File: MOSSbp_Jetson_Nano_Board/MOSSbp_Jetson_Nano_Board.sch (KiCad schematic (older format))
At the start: 13 parts, among them J1 24V, J2 Jetson_Nano_Dev, U1 LMR14020

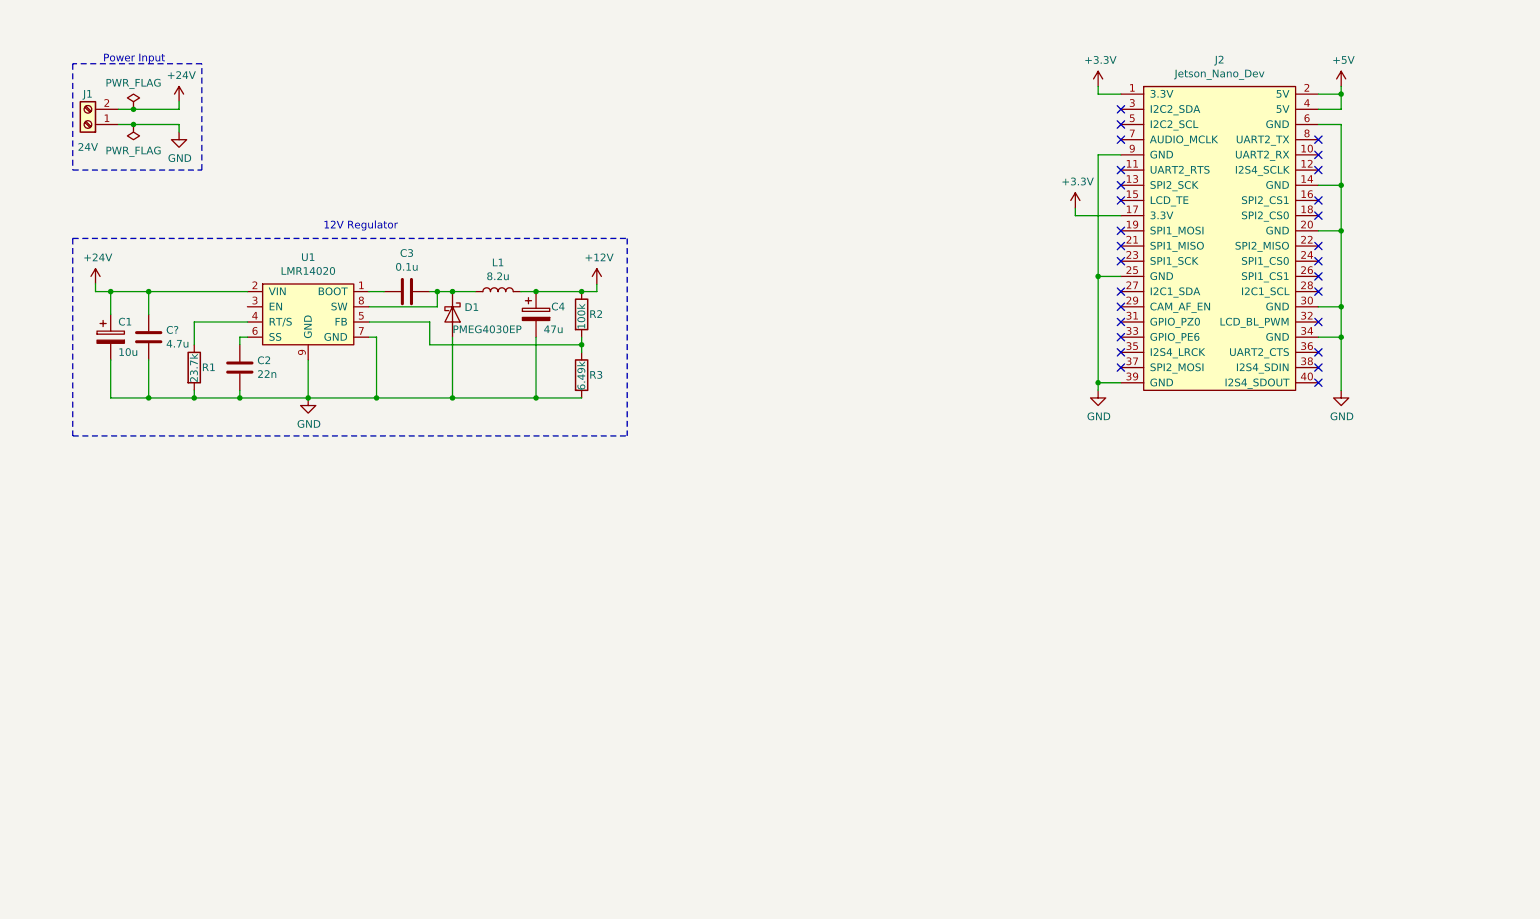
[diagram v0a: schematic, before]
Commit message: Added fans and pump controls
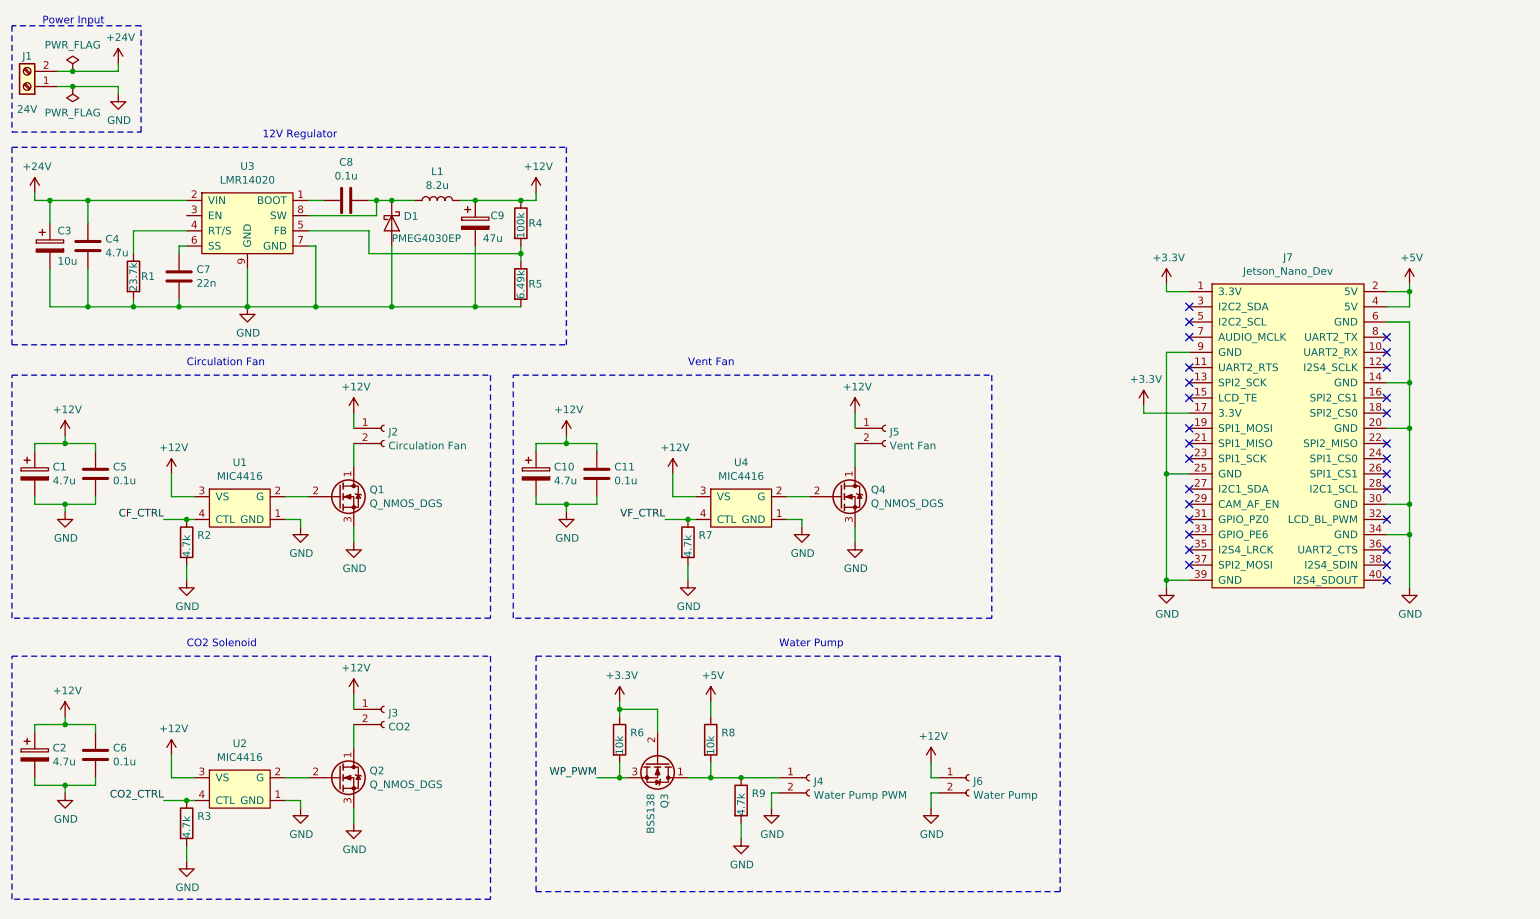
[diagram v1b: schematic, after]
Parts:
- added C1, C10, C2: 4.7u, symbol Device:CP
- added C11, C5, C6: 0.1u, symbol Device:C
- added J2: Circulation Fan, symbol Connector:Conn_01x02_Female
- added J3: CO2, symbol Connector:Conn_01x02_Female
- added J4: Water Pump PWM, symbol Connector:Conn_01x02_Female
- added J5: Vent Fan, symbol Connector:Conn_01x02_Female
- added J6: Water Pump, symbol Connector:Conn_01x02_Female
- added Q1, Q2, Q4: Q_NMOS_DGS, symbol Device:Q_NMOS_DGS
- added Q3: BSS138, symbol Device:Q_NMOS_DGS
- added R2, R3, R7, R9: 4.7k, symbol Device:R
- added R6, R8: 10k, symbol Device:R
- added U1, U2, U4: MIC4416, Package_TO_SOT_SMD:SOT-143, symbol rg_symbols:MIC4416
- gave numbers to parts that had none: 1
- renumbered C1 to C3, C2 to C7, C3 to C8, C4 to C9, J2 to J7, R2 to R4, R3 to R5, U1 to U3
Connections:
- net +12V: now also C1.1, C10.1, C11.1, C2.1, C5.1, C6.1, J2.1 (Pin_1), J3.1 (Pin_1), J5.1 (Pin_1), J6.1 (Pin_1), U1.3 (VS), U2.3 (VS), U4.3 (VS)
- net +3V3: now also Q3.2 (G), R6.1
- net +5V: now also R8.1
- net GND: now also C1.2, C10.2, C11.2, C2.2, C5.2, C6.2, J4.2 (Pin_2), J6.2 (Pin_2), Q1.3 (S), Q2.3 (S), Q4.3 (S), R2.2, R3.2, R7.2, R9.2, U1.1 (GND), U2.1 (GND), U4.1 (GND)
- new net: J2.2 (Pin_2), Q1.1 (D)
- new net: Q1.2 (G), U1.2 (G)
- new net: J5.2 (Pin_2), Q4.1 (D)
- new net: Q4.2 (G), U4.2 (G)
- new net: J3.2 (Pin_2), Q2.1 (D)
- new net: Q2.2 (G), U2.2 (G)
- new net: J4.1 (Pin_1), Q3.1 (D), R8.2, R9.1
- new net CF_CTRL: R2.1, U1.4 (CTL)
- new net CO2_CTRL: R3.1, U2.4 (CTL)
- new net VF_CTRL: R7.1, U4.4 (CTL)
- new net WP_PWM: Q3.3 (S), R6.2
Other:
- note added: "CO2 Solenoid"
- note added: "Circulation Fan"
- note added: "Vent Fan"
- note added: "Water Pump"
- moved on the sheet: C3, C4, C7, C8, C9, D1, J1, J7, L1, R1, R4, R5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

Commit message: Added 5V regulator and control pins
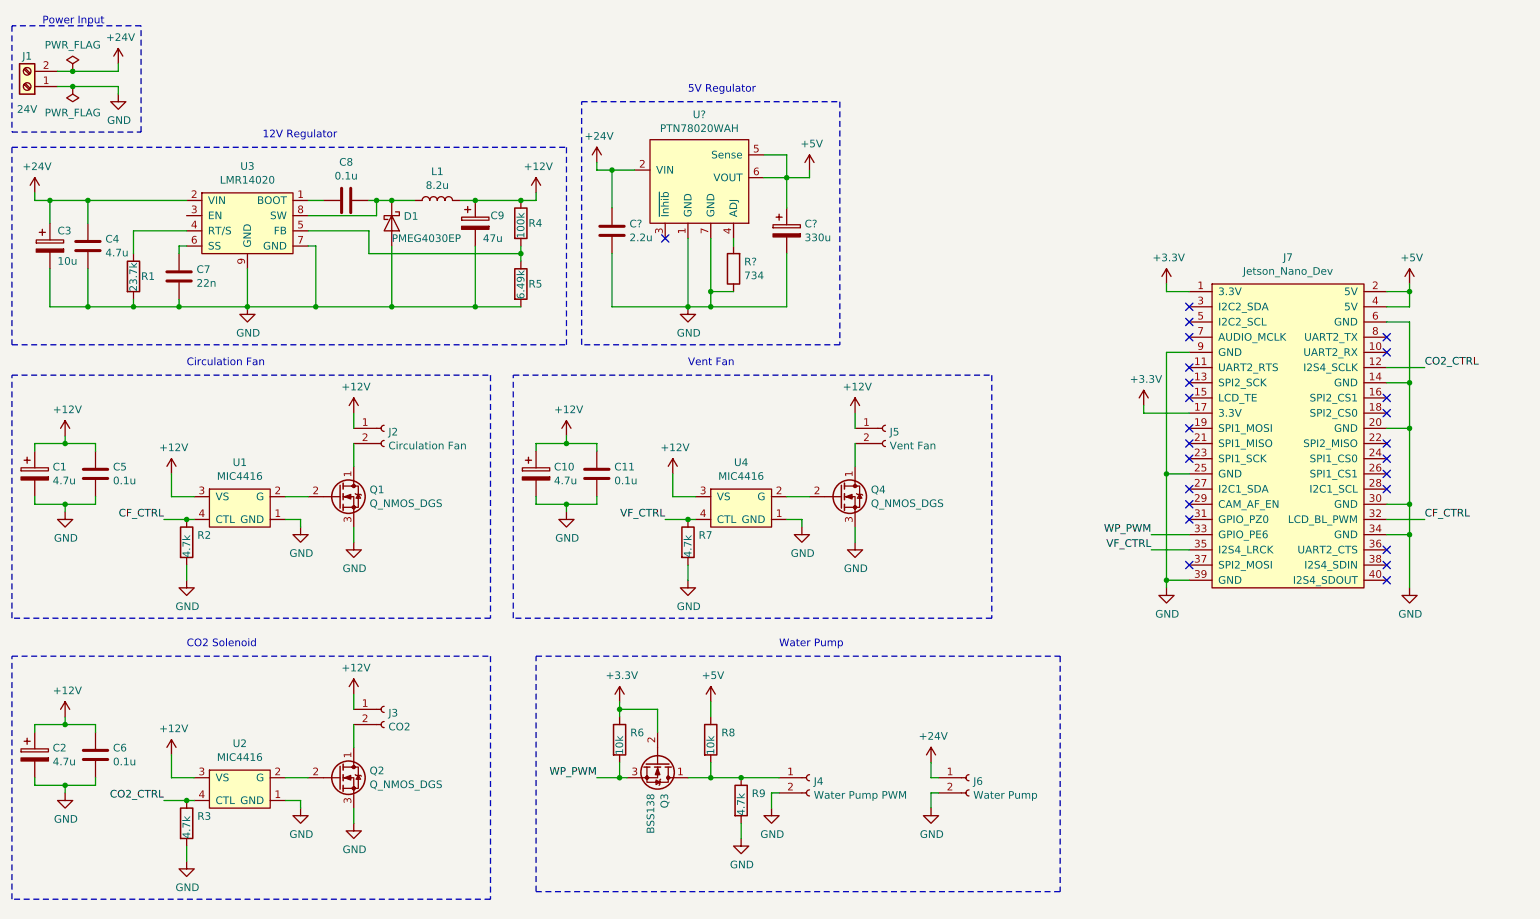
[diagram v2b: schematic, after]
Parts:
- added C?: 2.2u, symbol Device:C
- added C?: 330u, symbol Device:CP
- added R?: 734, symbol Device:R
- added U?: PTN78020WAH, RG_footprints:PTN78020WAH, symbol rg_symbols:PTN78020WAH
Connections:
- net +12V: no longer J6.1 (Pin_1)
- net +24V: now also J6.1 (Pin_1), C?.1, U?.2 (VIN)
- net +5V: now also C?.1, U?.5 (Sense), U?.6 (VOUT)
- net CF_CTRL: now also J7.32 (LCD_BL_PWM)
- net CO2_CTRL: now also J7.12 (I2S4_SCLK)
- net GND: now also C?.2, C?.2, R?.1, U?.1 (GND), U?.7 (GND)
- net VF_CTRL: now also J7.35 (I2S4_LRCK)
- net WP_PWM: now also J7.33 (GPIO_PE6)
- new net: R?.2, U?.4 (ADJ)
- no-connect marks 28 -> 25
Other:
- note added: "5V Regulator"
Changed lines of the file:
@@
 NoConn ~ 8350 3800
 NoConn ~ 8350 3900
-NoConn ~ 8350 4000
-NoConn ~ 8350 4100
 NoConn ~ 8350 4200
 NoConn ~ 9650 2700
 NoConn ~ 9650 2800
-NoConn ~ 9650 2900
 NoConn ~ 9650 3100
 NoConn ~ 9650 3200
@@
 NoConn ~ 9650 3600
 NoConn ~ 9650 3700
-NoConn ~ 9650 3900
 NoConn ~ 9650 4100
 NoConn ~ 9650 4200
@@
 	9800 2600 9800 3000
 Connection ~ 9800 3000
-$Comp
-L rg_symbols:Jetson_Nano_Dev J7
-U 1 1 5E099751
-P 7400 3300
-F 0 "J7" H 9000 4425 50  0000 C CNN
-F 1 "Jetson_Nano_Dev" H 9000 4334 50  0000 C CNN
-F 2 "Connector_PinHeader_2.54mm:PinHeader_2x20_P2.54mm_Vertical" H 9000 2100 50  0001 C CNN
-F 3 "~" H 8550 3300 50  0001 C CNN
-	1    7400 3300
-	1    0    0    -1
-$EndComp
 $Comp
 L Device:CP C3
@@
 $EndComp
 $Comp
-L power:+12V #PWR031
-U 1 1 5E3E58FB
-P 6650 5500
-F 0 "#PWR031" H 6650 5350 50  0001 C CNN
-F 1 "+12V" H 6665 5673 50  0000 C CNN
-F 2 "" H 6650 5500 50  0001 C CNN
-F 3 "" H 6650 5500 50  0001 C CNN
-	1    6650 5500
-	1    0    0    -1
-$EndComp
-$Comp
 L power:GND #PWR032
 U 1 1 5E3E5D52
@@
 Text Notes 5650 4750 0    50   ~ 0
 Water Pump
+$Comp
+L power:+24V #PWR?
+U 1 1 5E2B454C
+P 6650 5500
+F 0 "#PWR?" H 6650 5350 50  0001 C CNN
+F 1 "+24V" H 6665 5673 50  0000 C CNN
+F 2 "" H 6650 5500 50  0001 C CNN
+F 3 "" H 6650 5500 50  0001 C CNN
+	1    6650 5500
+	1    0    0    -1
+$EndComp
+$Comp
+L rg_symbols:PTN78020WAH U?
+U 1 1 5E2E2A70
+P 5100 1650
+F 0 "U?" H 5125 2065 50  0000 C CNN
+F 1 "PTN78020WAH" H 5125 1974 50  0000 C CNN
+F 2 "RG_footprints:PTN78020WAH" H 4650 1350 50  0001 C CNN
+F 3 "" H 4650 1350 50  0001 C CNN
+F 4 "296-20515-ND" H 5100 1650 50  0001 C CNN "Digi-Key_PN"
+	1    5100 1650
+	1    0    0    -1
+$EndComp
+$Comp
+L power:+24V #PWR?
+U 1 1 5E2EAD97
+P 4450 1550
+F 0 "#PWR?" H 4450 1400 50  0001 C CNN
+F 1 "+24V" H 4465 1723 50  0000 C CNN
+F 2 "" H 4450 1550 50  0001 C CNN
+F 3 "" H 4450 1550 50  0001 C CNN
+	1    4450 1550
+	1    0    0    -1
+$EndComp
+$Comp
+L Device:C C?
+U 1 1 5E2F15A4
+P 4550 2000
+F 0 "C?" H 4665 2046 50  0000 L CNN
+F 1 "2.2u" H 4665 1955 50  0000 L CNN
+F 2 "" H 4588 1850 50  0001 C CNN
+F 3 "~" H 4550 2000 50  0001 C CNN
+	1    4550 2000
+	1    0    0    -1
+$EndComp
+Wire Wire Line
+	5350 2100 5350 2050
+$Comp
+L Device:CP C?
+U 1 1 5E32825C
+P 5700 2000
+F 0 "C?" H 5818 2046 50  0000 L CNN
+F 1 "330u" H 5818 1955 50  0000 L CNN
+F 2 "" H 5738 1850 50  0001 C CNN
+F 3 "~" H 5700 2000 50  0001 C CNN
+	1    5700 2000
+	1    0    0    -1
+$EndComp
+$Comp
+L power:+5V #PWR?
+U 1 1 5E350252
+P 5850 1600
+F 0 "#PWR?" H 5850 1450 50  0001 C CNN
+F 1 "+5V" H 5865 1773 50  0000 C CNN
+F 2 "" H 5850 1600 50  0001 C CNN
+F 3 "" H 5850 1600 50  0001 C CNN
+	1    5850 1600
+	1    0    0    -1
+$EndComp
+$Comp
+L Device:R R?
+U 1 1 5E2F2841
+P 5350 2250
+F 0 "R?" H 5280 2204 50  0000 R CNN
+F 1 "734" H 5280 2295 50  0000 R CNN
+F 2 "" V 5280 2250 50  0001 C CNN
+F 3 "~" H 5350 2250 50  0001 C CNN
+	1    5350 2250
+	-1   0    0    1
+$EndComp
+Wire Wire Line
+	5050 2050 5050 2500
+Wire Wire Line
+	5050 2500 4550 2500
+Wire Wire Line
+	4550 2500 4550 2150
+Wire Wire Line
+	5700 2500 5700 2150
+Connection ~ 5050 2500
+Wire Wire Line
+	5550 1650 5700 1650
+Wire Wire Line
+	5700 1650 5700 1850
+Connection ~ 5700 1650
+Wire Wire Line
+	5550 1500 5700 1500
+Wire Wire Line
+	5700 1500 5700 1650
+Wire Wire Line
+	4550 1850 4550 1600
+Wire Wire Line
+	4550 1600 4700 1600
+Wire Wire Line
+	4450 1550 4450 1600
+Wire Wire Line
+	4450 1600 4550 1600
+Connection ~ 4550 1600
+Wire Wire Line
+	5700 1650 5850 1650
+Wire Wire Line
+	5850 1650 5850 1600
+$Comp
+L power:GND #PWR?
+U 1 1 5E3DE30B
+P 5050 2500
+F 0 "#PWR?" H 5050 2250 50  0001 C CNN
+F 1 "GND" H 5055 2327 50  0000 C CNN
+F 2 "" H 5050 2500 50  0001 C CNN
+F 3 "" H 5050 2500 50  0001 C CNN
+	1    5050 2500
+	1    0    0    -1
+$EndComp
+Wire Wire Line
+	5050 2500 5200 2500
+Wire Wire Line
+	5200 2500 5700 2500
+Connection ~ 5200 2500
+Wire Wire Line
+	5200 2050 5200 2400
+Wire Wire Line
+	5350 2400 5200 2400
+Connection ~ 5200 2400
+Wire Wire Line
+	5200 2400 5200 2500
+Wire Notes Line
+	4350 2750 4350 1150
+Wire Notes Line
+	4350 1150 6050 1150
+Wire Notes Line
+	6050 1150 6050 2750
+Wire Notes Line
+	6050 2750 4350 2750
+Text Notes 5050 1100 0    50   ~ 0
+5V Regulator
+NoConn ~ 4900 2050
+Wire Wire Line
+	8350 4000 8100 4000
+Text Label 8100 4000 2    50   ~ 0
+WP_PWM
+$Comp
+L rg_symbols:Jetson_Nano_Dev J7
+U 1 1 5E099751
+P 7400 3300
+F 0 "J7" H 9000 4425 50  0000 C CNN
+F 1 "Jetson_Nano_Dev" H 9000 4334 50  0000 C CNN
+F 2 "Connector_PinHeader_2.54mm:PinHeader_2x20_P2.54mm_Vertical" H 9000 2100 50  0001 C CNN
+F 3 "~" H 8550 3300 50  0001 C CNN
+	1    7400 3300
+	1    0    0    -1
+$EndComp
+Wire Wire Line
+	9650 3900 9900 3900
+Text Label 9900 3900 0    50   ~ 0
+CF_CTRL
+Wire Wire Line
+	8350 4100 8100 4100
+Text Label 8100 4100 2    50   ~ 0
+VF_CTRL
+Wire Wire Line
+	9650 2900 9900 2900
+Text Label 9900 2900 0    50   ~ 0
+CO2_CTRL
 $EndSCHEMATC

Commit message: Added I2C interface and assigned parts
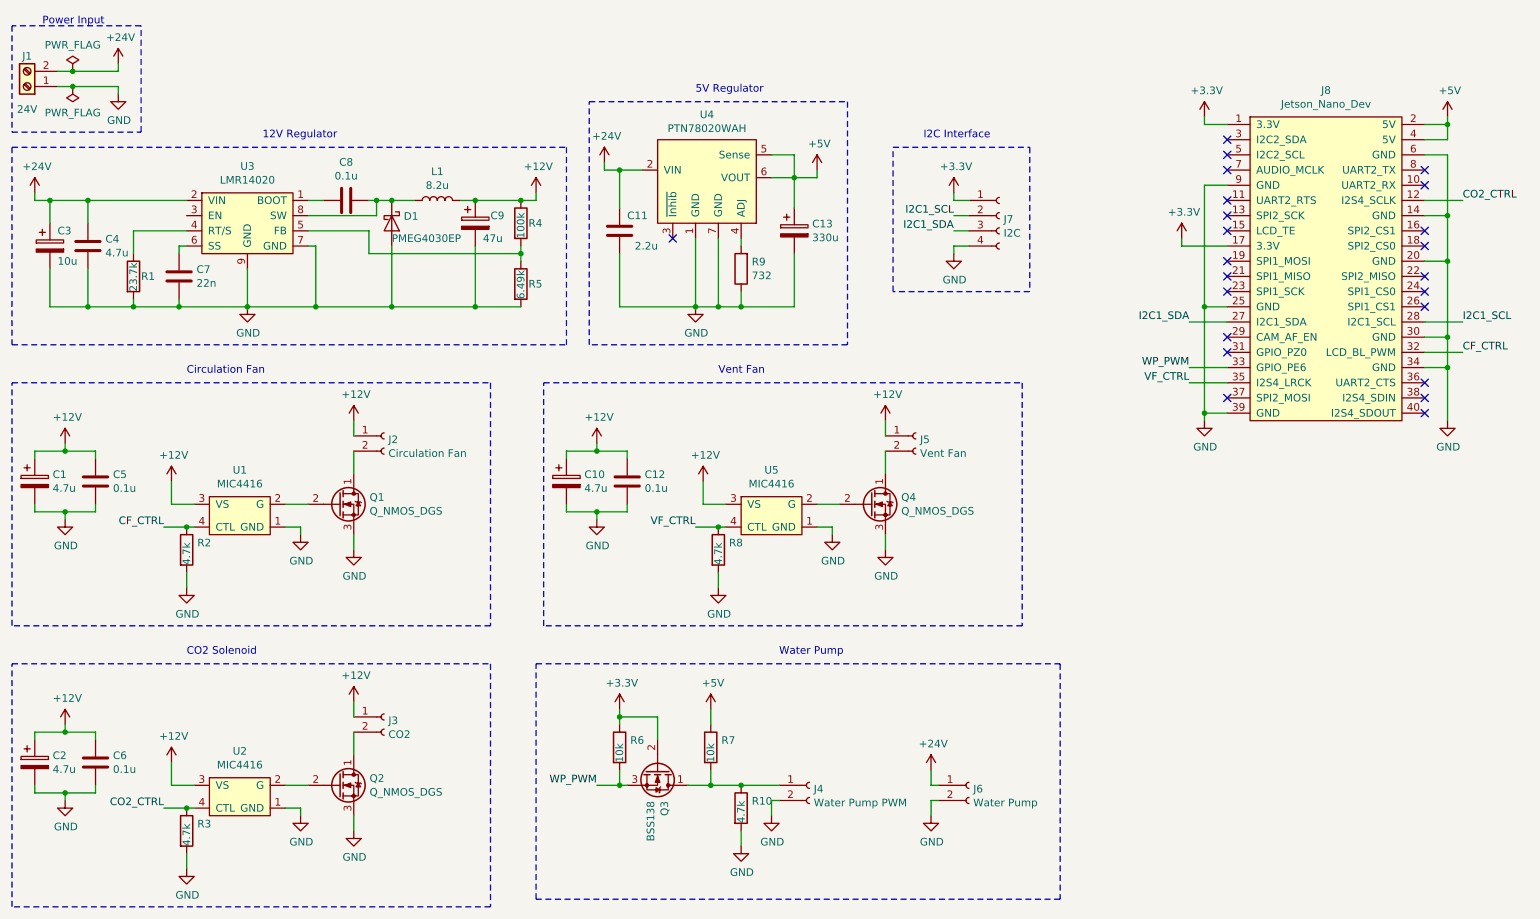
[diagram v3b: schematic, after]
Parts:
- added J7: I2C, Connector_JST:JST_GH_BM04B-GHS-TBT_1x04-1MP_P1.25mm_Vertical, symbol Connector:Conn_01x04_Female
- J2, J3, J5: footprint (none) -> Connector_JST:JST_GH_BM02B-GHS-TBT_1x02-1MP_P1.25mm_Vertical; Digi-Key_PN (none) -> 455-1578-1-ND
- Q1, Q2, Q3, Q4: footprint (none) -> Package_TO_SOT_SMD:SOT-23
- R9: renamed from R?; value 734 -> 732
- gave numbers to parts that had none: 3
- renumbered C11 to C12, J7 to J8, R9 to R10, R8 to R7, R7 to R8, U4 to U5
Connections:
- net +3V3: now also J7.1 (Pin_1)
- net GND: now also J7.4 (Pin_4)
- net I2C1_SDA: now reaches J8.27 (I2C1_SDA)
- net I2C1_SDA: now also J7.3 (Pin_3)
- net I2C1_SCL: now reaches J8.28 (I2C1_SCL)
- net I2C1_SCL: now also J7.2 (Pin_2)
- no-connect marks 25 -> 23
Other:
- note added: "I2C Interface"
- moved on the sheet: C1, C10, C11, C12, C13, C2, C5, C6, J2, J3, J4, J5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
